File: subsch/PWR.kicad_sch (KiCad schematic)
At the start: 3 parts, among them U11 HX9193

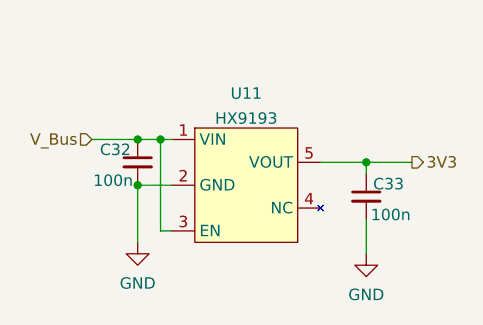
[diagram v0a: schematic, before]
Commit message: Change routings&Add ESD for UART and CAN&Add 5V protection and pull-resistance for GPIO
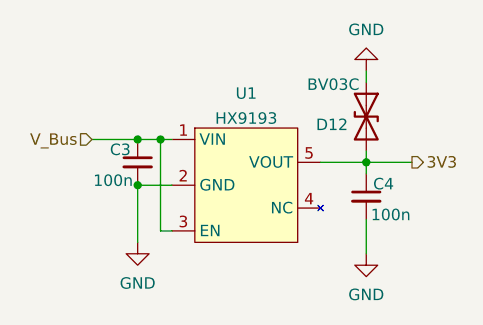
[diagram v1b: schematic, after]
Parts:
- added D12: BV03C, Diode_SMD:D_SOD-323, symbol Device:D_TVS
- renumbered C32 to C3, C33 to C4, U11 to U1
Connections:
- net 3V3: now also D12.2 (A2)
- net GND: now also D12.1 (A1)
